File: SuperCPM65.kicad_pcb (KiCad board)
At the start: 2 copper layers, 98.5 x 79.5 mm, 43 parts, among them CON1 db_vgparts_SNES-EDGE, J1 Conn_01x02, J2 Conn_01x06, J3 Conn_01x06, J4 GSD090012SEU, J5 Mini-DIN-6, U1 74HC14, U2 PIC12F629-IP, U3 SST39SF010, U4 W65C22NxP, U5 74HC595, U6 74HC595, U7 TXB0104D, U8 AP2205-33W5-7

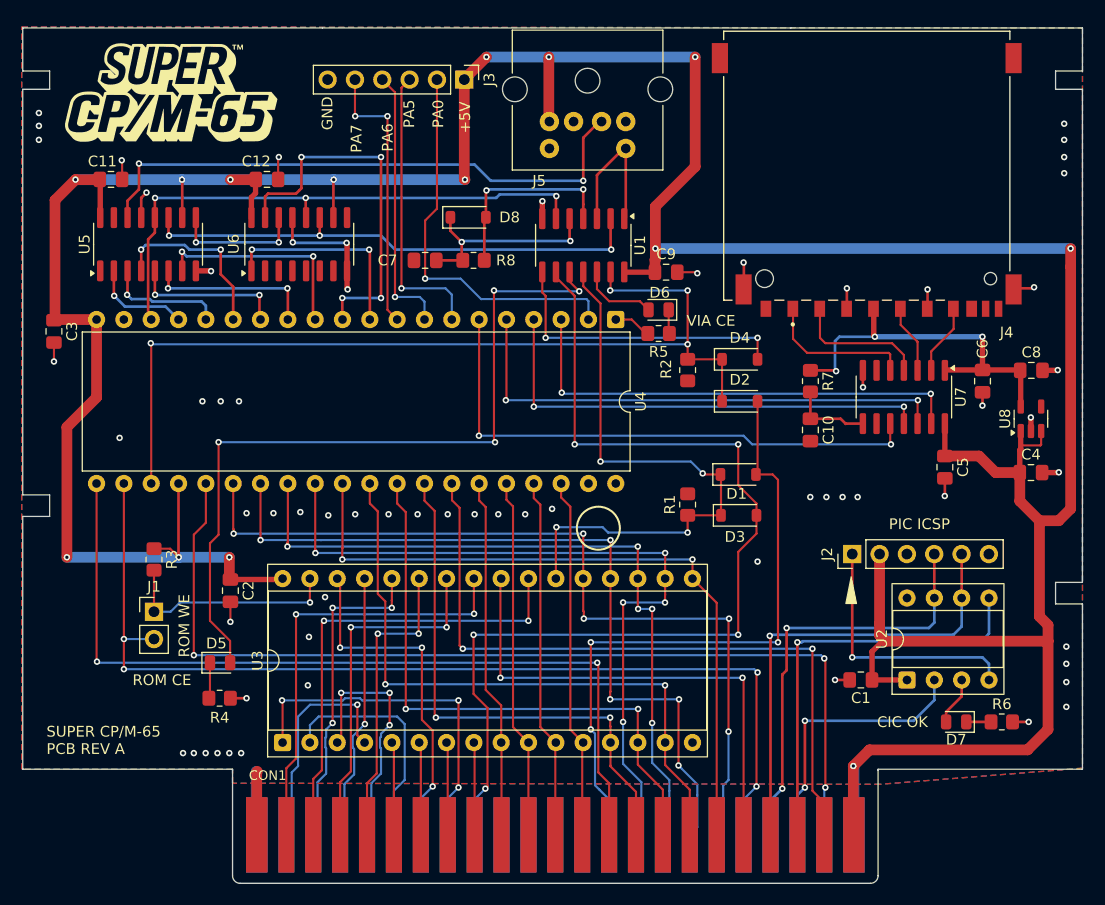
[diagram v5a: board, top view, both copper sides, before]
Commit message: Imported schematic updated, placed LEDs at top, minor rearrangement
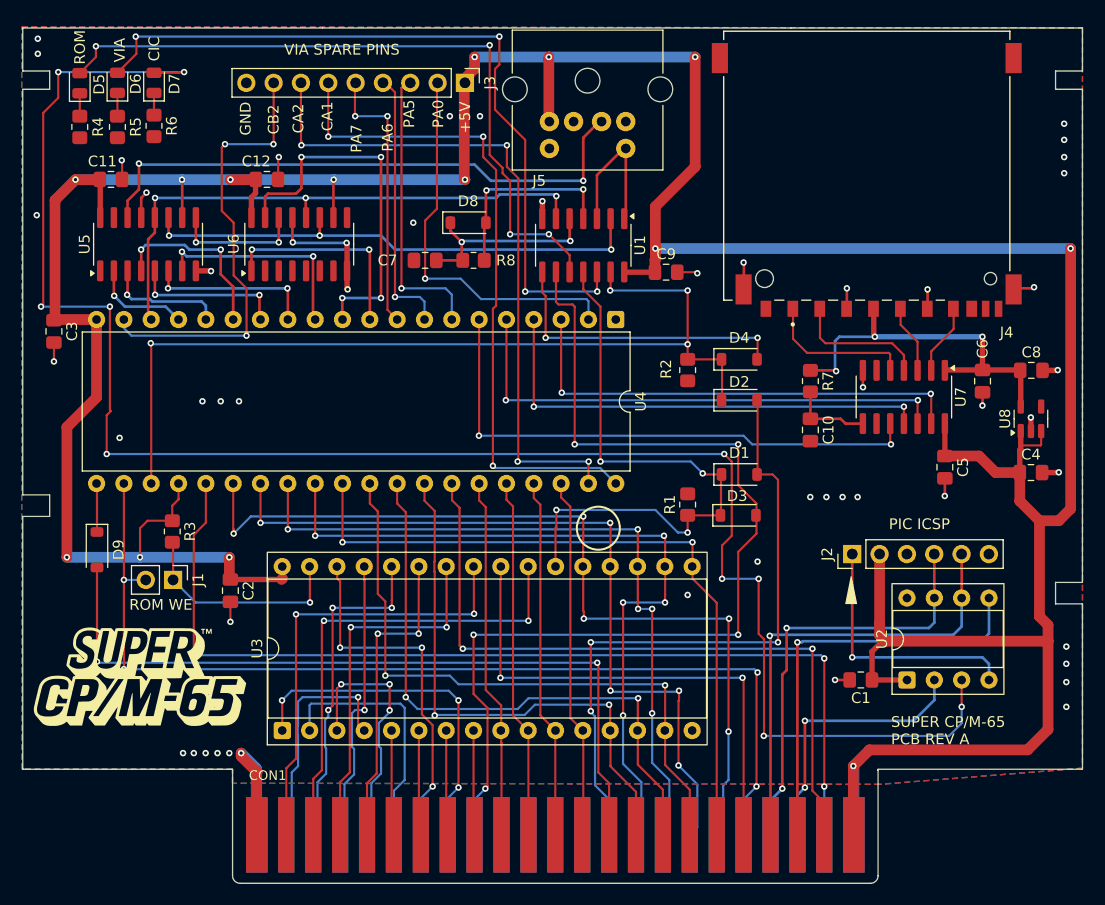
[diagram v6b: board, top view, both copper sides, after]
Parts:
- added D9: BAT42W-V, Diode_SMD:D_SOD-123, F.Cu at (70.9, 90.5)
- D1, D2, D3, D4, D8: value 1N4148W -> BAT42W-V
- J3: value Conn_01x06 -> Conn_01x09; footprint Connector_PinHeader_2.54mm:PinHeader_1x06_P2.54mm_Vertical -> Connector_PinHeader_2.54mm:PinHeader_1x09_P2.54mm_Vertical
- moved R6 96.3 mm to (76.2, 51.1), turned to -90 degrees
- moved D7 95.3 mm to (76.2, 47.1), turned to 90 degrees
- moved D5 55.4 mm to (69.3, 47.1), turned to 90 degrees
- moved R4 54.7 mm to (69.3, 51.2), turned to -90 degrees
- moved D6 54.5 mm to (72.8, 47.1), turned to 90 degrees
- moved G*** 54.4 mm to (74.8, 103.1)
- moved R5 53.8 mm to (72.8, 51.2), turned to -90 degrees
- moved J1 3.45 mm to (78.0, 93.3), turned to -90 degrees
- moved R3 3.11 mm to (77.9, 88.8)
- moved U3 1.12 mm to (88.1, 107.3)
- moved D8 0.50 mm to (105.4, 60.1)
- moved J3 0.31 mm to (105.1, 47.1)
- moved D2 0.11 mm to (130.6, 76.6)
- moved D1 0.10 mm to (130.6, 83.5)
- moved D3 0.05 mm to (130.5, 87.3)
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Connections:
- J3 pad 6: GND -> /CA1
- U4 pad 19: unconnected-(U4-CB2-Pad19) -> /CB2
- U4 pad 21: ~{IRQ} -> Net-(D9-K)
- U4 pad 39: unconnected-(U4-CA2-Pad39) -> /CA2
- U4 pad 40: unconnected-(U4-CA1-Pad40) -> /CA1
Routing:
- net Net-(D7-A): track 4.49 -> 168.1 mm, vias 0 -> 10
- net Net-(D6-A): track 7.19 -> 71.5 mm, vias 0 -> 4
- net /CA2: track 0.00 -> 63.6 mm, vias 0 -> 4
- net /CA1: track 0.00 -> 62.7 mm, vias 0 -> 3
- net /CB2: track 0.00 -> 41.6 mm, vias 0 -> 3
- net ~{IRQ}: track 79.6 -> 71.7 mm
- net Net-(D5-A): track 71.6 -> 66.0 mm
- net Net-(D9-K): track 0.00 -> 4.53 mm
- net /D7: track 79.3 -> 81.5 mm
- net GND: track 63.0 -> 61.1 mm, vias 65 -> 52
- net /BA0: track 21.8 -> 23.6 mm
- net /A14: track 24.9 -> 26.6 mm
- net /D0: track 50.3 -> 51.8 mm
- net Net-(D5-K): track 3.34 -> 2.12 mm
- net ~{RD}: track 46.4 -> 47.6 mm
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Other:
- board text added: "CA1"
- board text added: "CA2"
- board text added: "CB2"
- board text added: "CIC"
- board text added: "ROM"
- board text added: "VIA"
- board text added: "VIA SPARE PINS"
- board text removed: "CIC OK"
- board text removed: "ROM CE"
- board text removed: "VIA CE"
